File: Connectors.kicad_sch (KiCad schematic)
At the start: 9 parts, among them J14 200528-0100, J15 200528-0100, J16 200528-0100, J17 1824543, J18 200528-0100, J19 200528-0100, J2 200528-0100, J4 200528-0100, J9 200528-0100

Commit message: temp
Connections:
- net GND: no longer J15.6 (Pin_6), J15.8 (Pin_8)
- net MCU_RX_JETSON renamed Jetson_MISO
- net MCU_TX_JETSON renamed Jetson_MOSI
- new net Jetson_CLK: J15.8 (Pin_8)
- new net Jetson_CSn: J15.6 (Pin_6)
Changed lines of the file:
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@@
-	)
-	(junction
-		(at 157.48 49.53)
-		(diameter 0)
-		(color 0 0 0 0)
 	)
 	(junction
@@
 	)
 	(junction
-		(at 157.48 54.61)
-		(diameter 0)
-		(color 0 0 0 0)
-	)
-	(junction
 		(at 255.27 57.15)
 		(diameter 0)
@@
 	(wire
 		(pts
+			(xy 135.89 54.61) (xy 139.7 54.61)
+		)
+		(stroke
+			(width 0)
+			(type default)
+		)
+	)
+	(wire
+		(pts
 			(xy 203.2 110.49) (xy 203.2 113.03)
 		)
@@
 	(wire
 		(pts
-			(xy 157.48 49.53) (xy 157.48 54.61)
-		)
-		(stroke
-			(width 0)
-			(type default)
-		)
-	)
-	(wire
-		(pts
-			(xy 157.48 54.61) (xy 157.48 59.69)
+			(xy 157.48 46.99) (xy 157.48 59.69)
 		)
 		(stroke
@@
 	(wire
 		(pts
+			(xy 135.89 49.53) (xy 139.7 49.53)
+		)
+		(stroke
+			(width 0)
+			(type default)
+		)
+	)
+	(wire
+		(pts
 			(xy 87.63 154.94) (xy 87.63 157.48)
 		)
@@
 	(wire
 		(pts
-			(xy 135.89 49.53) (xy 157.48 49.53)
-		)
-		(stroke
-			(width 0)
-			(type default)
-		)
-	)
-	(wire
-		(pts
 			(xy 233.68 59.69) (xy 255.27 59.69)
 		)
@@
 	(wire
 		(pts
-			(xy 135.89 54.61) (xy 157.48 54.61)
-		)
-		(stroke
-			(width 0)
-			(type default)
-		)
-	)
-	(wire
-		(pts
 			(xy 138.43 110.49) (xy 152.4 110.49)
 		)
@@
 		(pts
 			(xy 39.37 175.26) (xy 36.83 175.26)
-		)
-		(stroke
-			(width 0)
-			(type default)
-		)
-	)
-	(wire
-		(pts
-			(xy 157.48 46.99) (xy 157.48 49.53)
 		)
 		(stroke
@@
 		)
 	)
+	(hierarchical_label "Jetson_CSn"
+		(shape input)
+		(at 139.7 49.53 0)
+		(fields_autoplaced yes)
+		(effects
+			(font
+				(size 1.27 1.27)
+			)
+			(justify left)
+		)
+	)
 	(hierarchical_label "I2C0_SCL"
 		(shape bidirectional)
 		(at 39.37 177.8 0)
+		(fields_autoplaced yes)
+		(effects
+			(font
+				(size 1.27 1.27)
+			)
+			(justify left)
+		)
+	)
+	(hierarchical_label "Jetson_CLK"
+		(shape input)
+		(at 139.7 54.61 0)
 		(fields_autoplaced yes)
 		(effects
@@
 		)
 	)
-	(hierarchical_label "I2C1_SDA"
-		(shape bidirectional)
-		(at 90.17 123.19 0)
-		(fields_autoplaced yes)
-		(effects
-			(font
-				(size 1.27 1.27)
-			)
-			(justify left)
-		)
-	)
-	(hierarchical_label "MCU_RX_JETSON"
+	(hierarchical_label "Jetson_MISO"
 		(shape output)
 		(at 139.7 57.15 0)
+		(fields_autoplaced yes)
+		(effects
+			(font
+				(size 1.27 1.27)
+			)
+			(justify left)
+		)
+	)
+	(hierarchical_label "I2C1_SDA"
+		(shape bidirectional)
+		(at 90.17 123.19 0)
+		(fields_autoplaced yes)
+		(effects
+			(font
+				(size 1.27 1.27)
+			)
+			(justify left)
+		)
+	)
+	(hierarchical_label "Jetson_MOSI"
+		(shape input)
+		(at 139.7 52.07 0)
 		(fields_autoplaced yes)
 		(effects
@@
 		(fields_autoplaced yes)
 		(effects
-			(font
-				(size 1.27 1.27)
-			)
-			(justify left)
-		)
-	)
-	(hierarchical_label "MCU_TX_JETSON"
-		(shape input)
-		(at 139.7 52.07 0)
-		(fields_autoplaced yes)
-		(effects

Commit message: v1 done
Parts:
- added J6: 200528-0100, Argus-Connectors:Molex_200528-0100_1x10-1MP_P1.00mm_Horizontal, symbol Connector_Generic_MountingPin:Conn_01x10_MountingPin
- J14, J15, J16, J18, J19, J2, J4, J9: footprint Connector_FFC-FPC:Molex_200528-0100_1x10-1MP_P1.00mm_Horizontal -> Argus-Connectors:Molex_200528-0100_1x10-1MP_P1.00mm_Horizontal
- J17: symbol MainBoard:1824543 -> Argus-Connectors:1824543
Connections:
- net +3V3: now also J6.2 (Pin_2), J6.3 (Pin_3)
- net GND: now also J6.4 (Pin_4), J6.MP (MountPin)
- net I2C0_SCL: now also J6.10 (Pin_10)
- net I2C0_SDA: now also J6.9 (Pin_9)
- net Jetson_CSn: now also J15.7 (Pin_7); no longer J15.6 (Pin_6)
- net Jetson_MISO: now also J15.6 (Pin_6); no longer J15.9 (Pin_9)
- net Jetson_MOSI: now also J15.9 (Pin_9); no longer J15.7 (Pin_7)
- net VSYS: now also J6.1 (Pin_1)
- net Battery_ALERT: no longer names the net of J19.7 (Pin_7)
- net Jetson_EN: no longer names the net of J15.4 (Pin_4)
- new net RX+: J6.8 (Pin_8)
- new net RX-: J6.7 (Pin_7)
- new net TX+: J6.5 (Pin_5)
- new net TX-: J6.6 (Pin_6)
- no-connect marks 0 -> 2

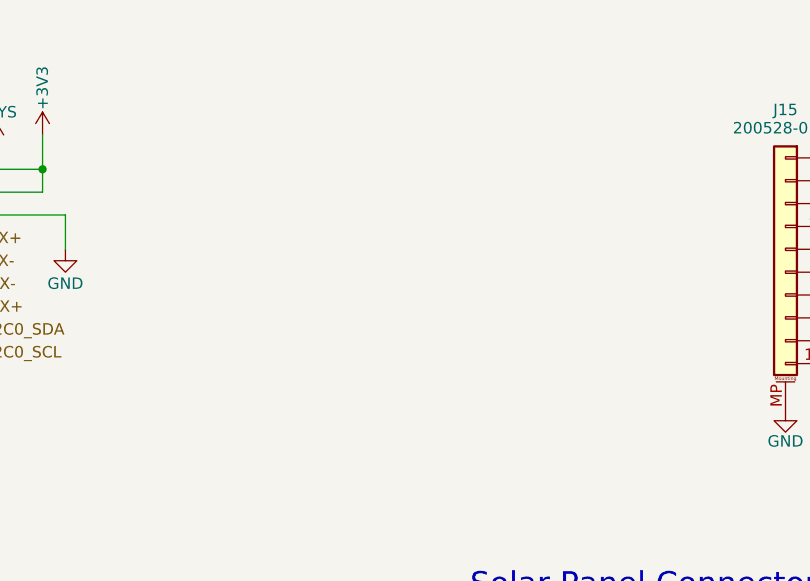
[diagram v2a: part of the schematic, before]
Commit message: Updated i2c device addresses and mcu caps
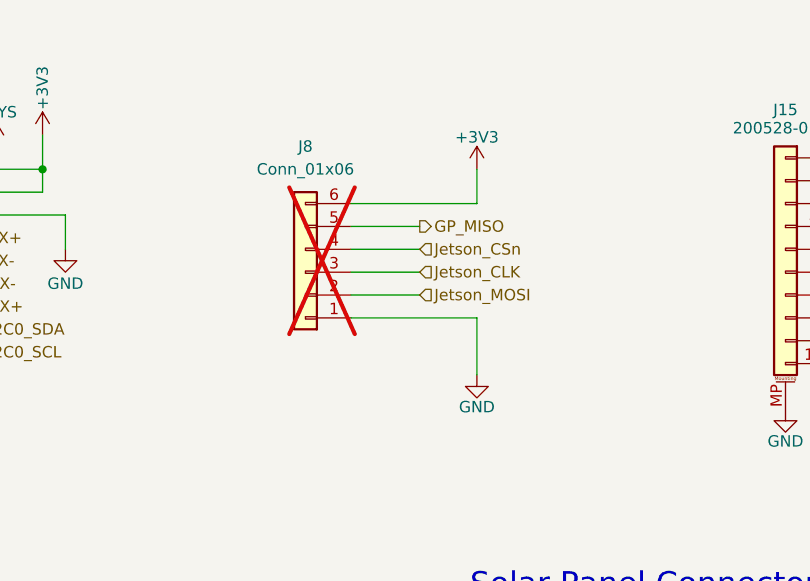
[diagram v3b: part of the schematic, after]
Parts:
- added J8: Conn_01x06, symbol Connector_Generic:Conn_01x06
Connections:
- net +3V3: now also J8.6 (Pin_6)
- net GND: now also J8.1 (Pin_1)
- net Jetson_CLK: now also J8.3 (Pin_3)
- net Jetson_CSn: now also J8.4 (Pin_4)
- net Jetson_MOSI: now also J8.2 (Pin_2)
- new net GP_MISO: J8.5 (Pin_5)

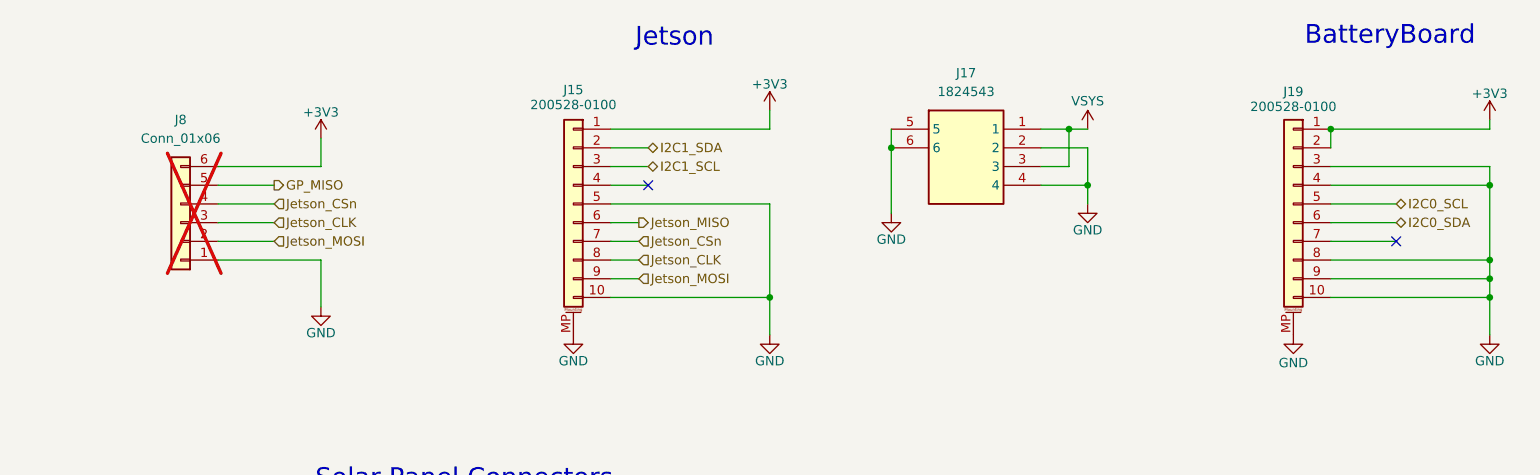
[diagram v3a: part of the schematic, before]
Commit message: Added extra connector
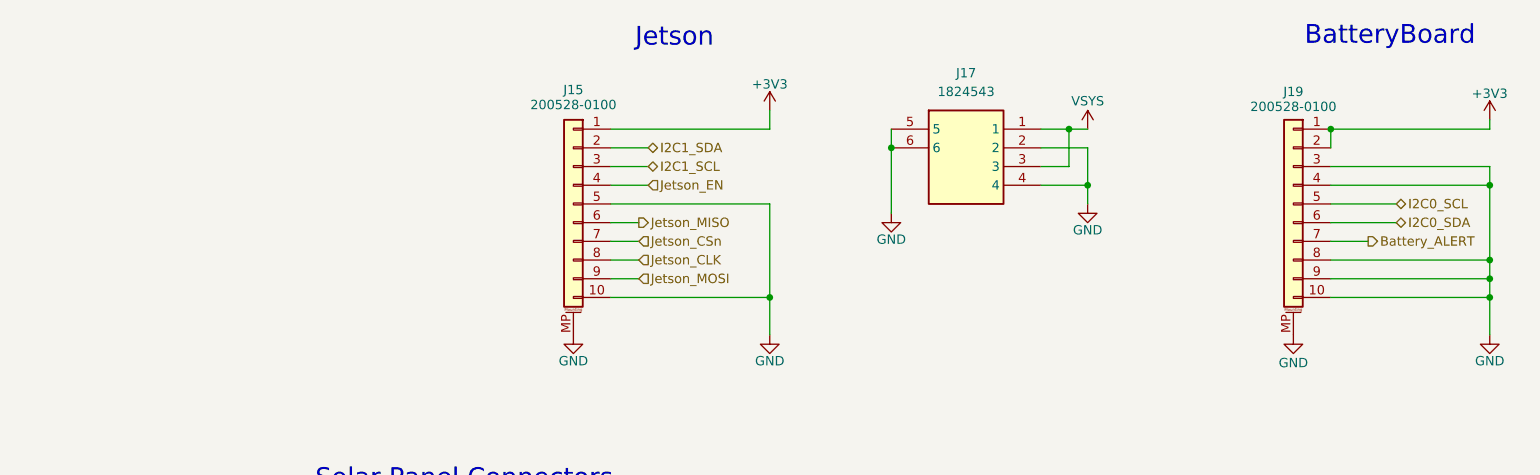
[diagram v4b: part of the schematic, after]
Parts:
- removed J8: Conn_01x06, symbol Connector_Generic:Conn_01x06
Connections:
- net Jetson_EN: now reaches J15.4 (Pin_4)
- net Battery_ALERT: now reaches J19.7 (Pin_7)
- no-connect marks 2 -> 0

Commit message: Updated connector locations
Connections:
- net +3V3: now also J15.2 (Pin_2), J16.1 (Pin_1), J19.7 (Pin_7), J19.8 (Pin_8); no longer J16.7 (Pin_7), J16.8 (Pin_8), J19.1 (Pin_1), J19.2 (Pin_2)
- net Battery_ALERT: now also J15.7 (Pin_7); no longer J19.7 (Pin_7)
- net GND: now also J15.3 (Pin_3), J15.4 (Pin_4), J15.8 (Pin_8), J15.9 (Pin_9), J16.10 (Pin_10), J19.5 (Pin_5), J19.6 (Pin_6); no longer J15.5 (Pin_5), J16.4 (Pin_4), J16.6 (Pin_6), J19.10 (Pin_10), J19.3 (Pin_3), J19.8 (Pin_8), J19.9 (Pin_9)
- net I2C0_SCL: now also J19.10 (Pin_10); no longer J19.5 (Pin_5)
- net I2C0_SDA: now also J19.9 (Pin_9); no longer J19.6 (Pin_6)
- net I2C1_SCL: now also J15.5 (Pin_5), J16.3 (Pin_3); no longer J15.3 (Pin_3), J16.10 (Pin_10)
- net I2C1_SDA: now also J15.6 (Pin_6), J16.2 (Pin_2); no longer J15.2 (Pin_2), J16.9 (Pin_9)
- net Jetson_CLK: now also J16.8 (Pin_8); no longer J15.8 (Pin_8)
- net Jetson_CSn: now also J16.7 (Pin_7); no longer J15.7 (Pin_7)
- net Jetson_EN: now also J16.4 (Pin_4); no longer J15.4 (Pin_4)
- net Jetson_MISO: now also J16.6 (Pin_6); no longer J15.6 (Pin_6)
- net Jetson_MOSI: now also J16.9 (Pin_9); no longer J15.9 (Pin_9)
- net VSYS: now also J19.1 (Pin_1), J19.2 (Pin_2), J19.3 (Pin_3); no longer J16.1 (Pin_1), J16.2 (Pin_2), J16.3 (Pin_3)
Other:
- note added: "CAMERA"

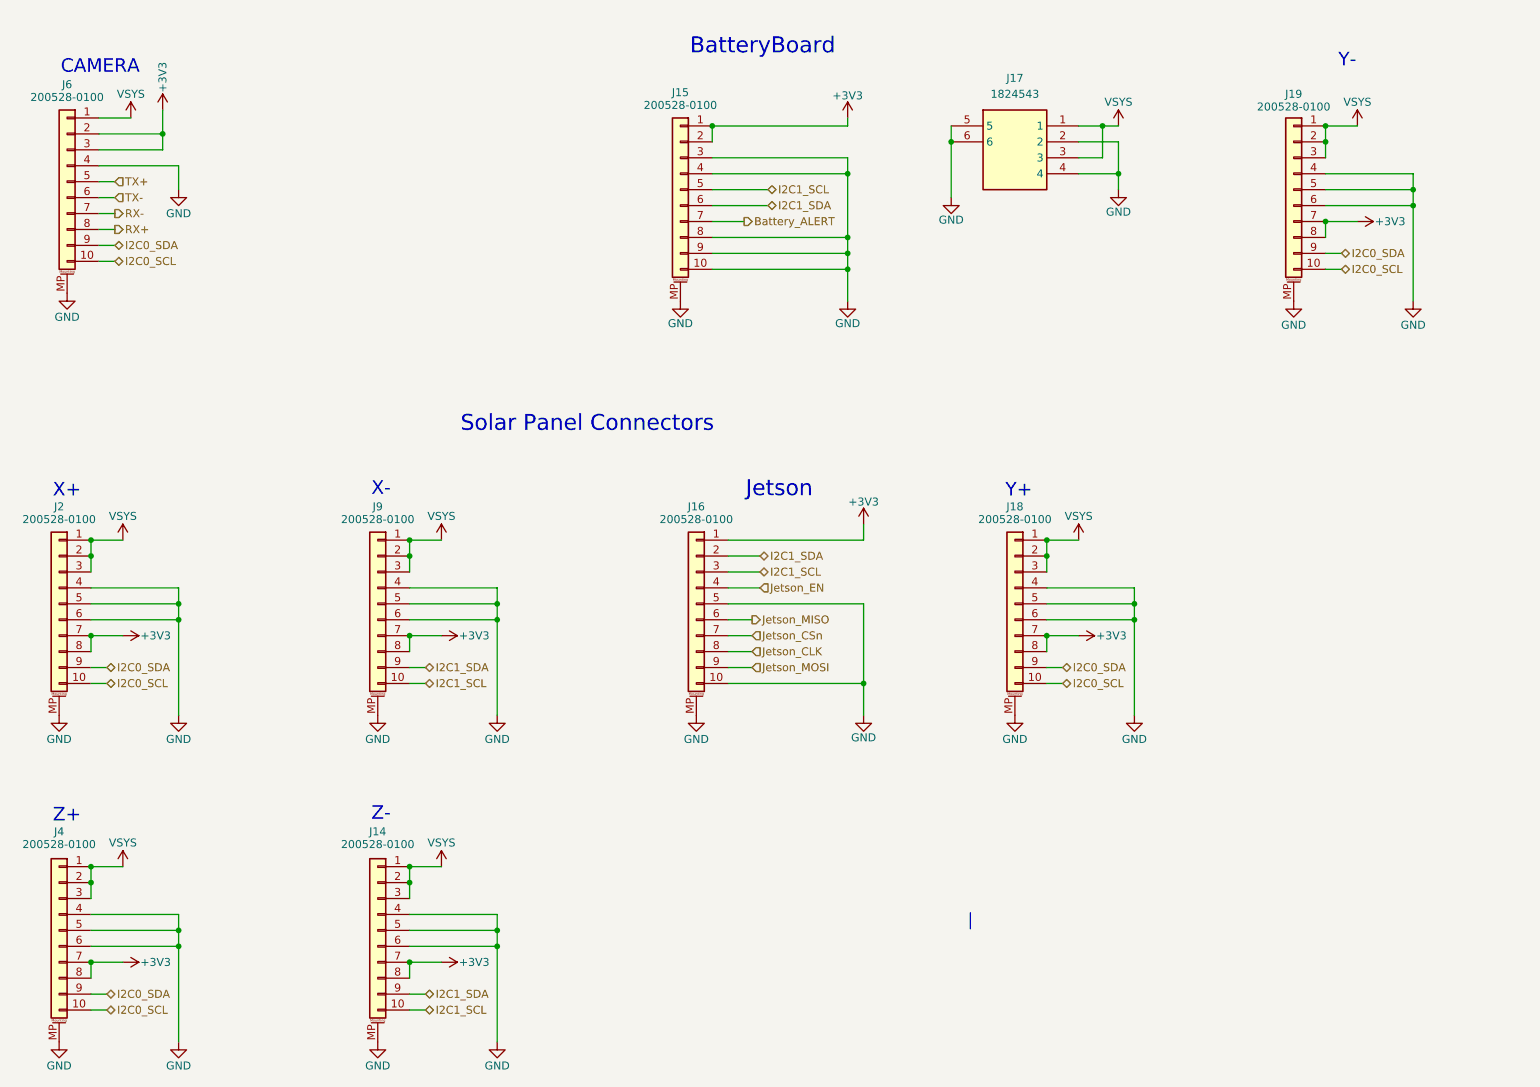
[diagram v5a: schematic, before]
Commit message: Fixed schematic bugs and corresponding layout modifications
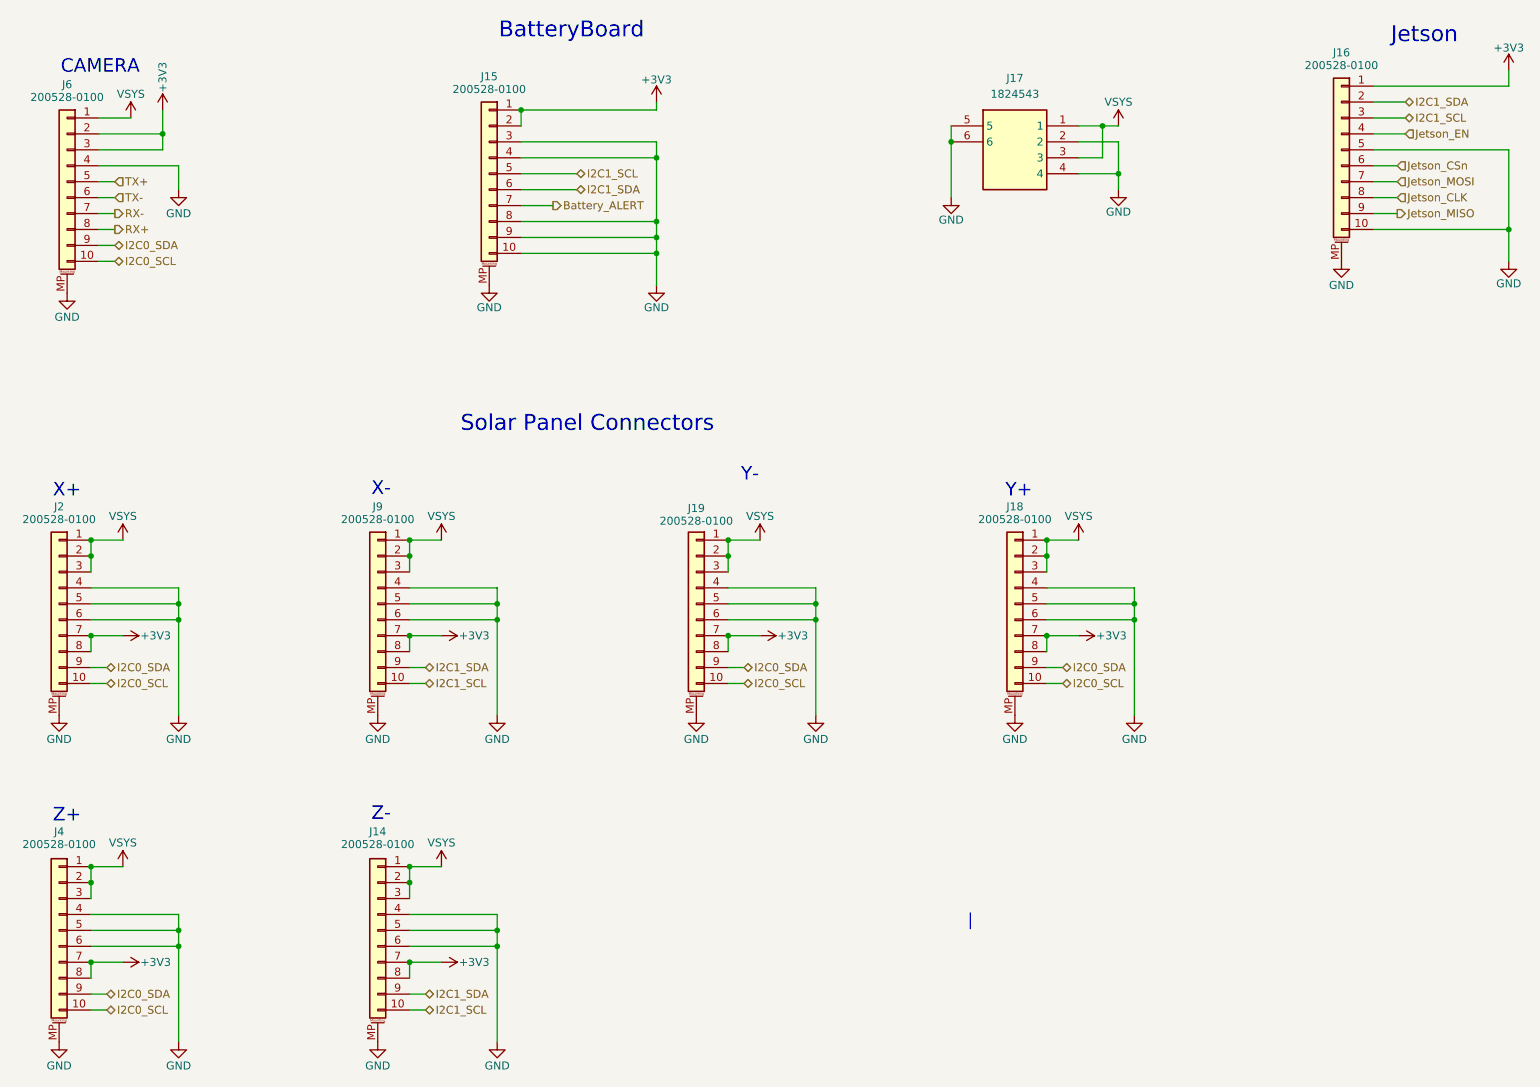
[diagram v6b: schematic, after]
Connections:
- net Jetson_CSn: now also J16.6 (Pin_6); no longer J16.7 (Pin_7)
- net Jetson_MISO: now also J16.9 (Pin_9); no longer J16.6 (Pin_6)
- net Jetson_MOSI: now also J16.7 (Pin_7); no longer J16.9 (Pin_9)
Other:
- moved on the sheet: J15, J16, J19

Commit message: Updated connector locations and types
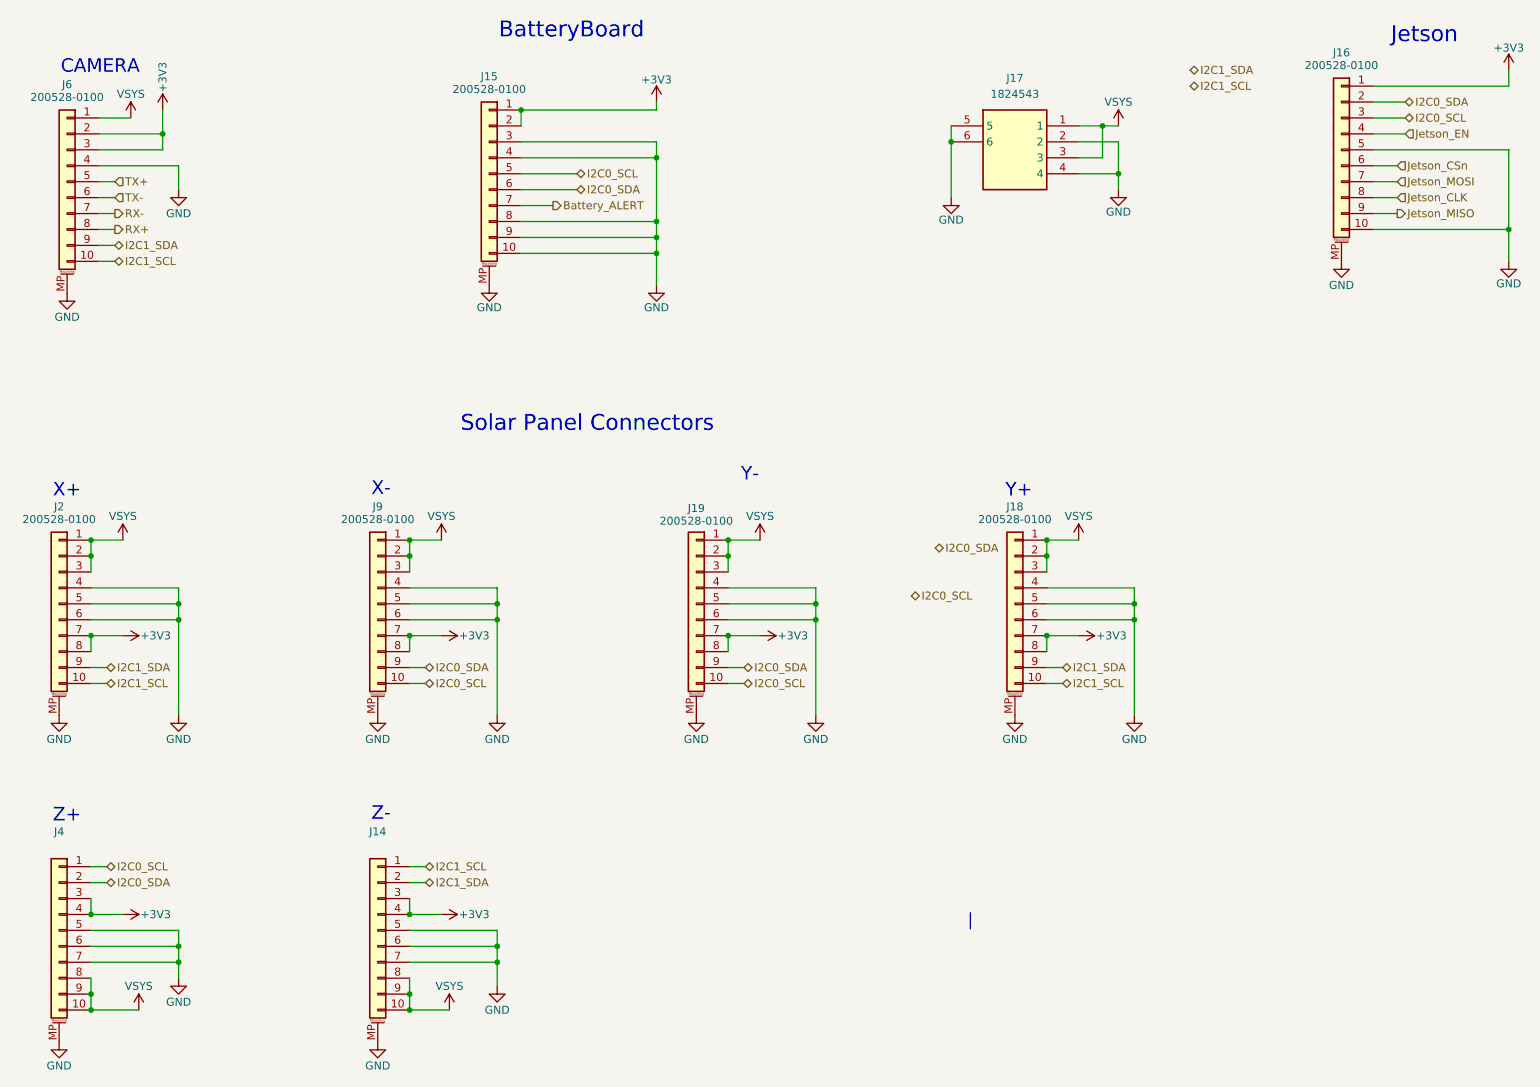
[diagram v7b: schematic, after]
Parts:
- J17: footprint Argus-Connectors:1824543 -> Argus-Connectors:1823654
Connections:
- net +3V3: now also J14.3 (Pin_3), J14.4 (Pin_4), J4.3 (Pin_3), J4.4 (Pin_4); no longer J14.7 (Pin_7), J14.8 (Pin_8), J4.7 (Pin_7), J4.8 (Pin_8)
- net GND: now also J14.7 (Pin_7), J4.7 (Pin_7); no longer J14.4 (Pin_4), J4.4 (Pin_4)
- net I2C0_SCL: now also J15.5 (Pin_5), J16.3 (Pin_3), J4.1 (Pin_1), J9.10 (Pin_10); no longer J18.10 (Pin_10), J2.10 (Pin_10), J4.10 (Pin_10), J6.10 (Pin_10)
- net I2C0_SDA: now also J15.6 (Pin_6), J16.2 (Pin_2), J4.2 (Pin_2), J9.9 (Pin_9); no longer J18.9 (Pin_9), J2.9 (Pin_9), J4.9 (Pin_9), J6.9 (Pin_9)
- net I2C1_SCL: now also J14.1 (Pin_1), J18.10 (Pin_10), J2.10 (Pin_10), J6.10 (Pin_10); no longer J14.10 (Pin_10), J15.5 (Pin_5), J16.3 (Pin_3), J9.10 (Pin_10)
- net I2C1_SDA: now also J14.2 (Pin_2), J18.9 (Pin_9), J2.9 (Pin_9), J6.9 (Pin_9); no longer J14.9 (Pin_9), J15.6 (Pin_6), J16.2 (Pin_2), J9.9 (Pin_9)
- net VSYS: now also J14.10 (Pin_10), J14.8 (Pin_8), J14.9 (Pin_9), J4.10 (Pin_10), J4.8 (Pin_8), J4.9 (Pin_9); no longer J14.1 (Pin_1), J14.2 (Pin_2), J14.3 (Pin_3), J4.1 (Pin_1), J4.2 (Pin_2), J4.3 (Pin_3)
